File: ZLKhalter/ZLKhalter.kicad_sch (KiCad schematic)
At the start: 4 parts, among them J1 Conn_02x04_Counter_Clockwise, J2 Conn_01x04_Pin, J3 Conn_02x04_Counter_Clockwise

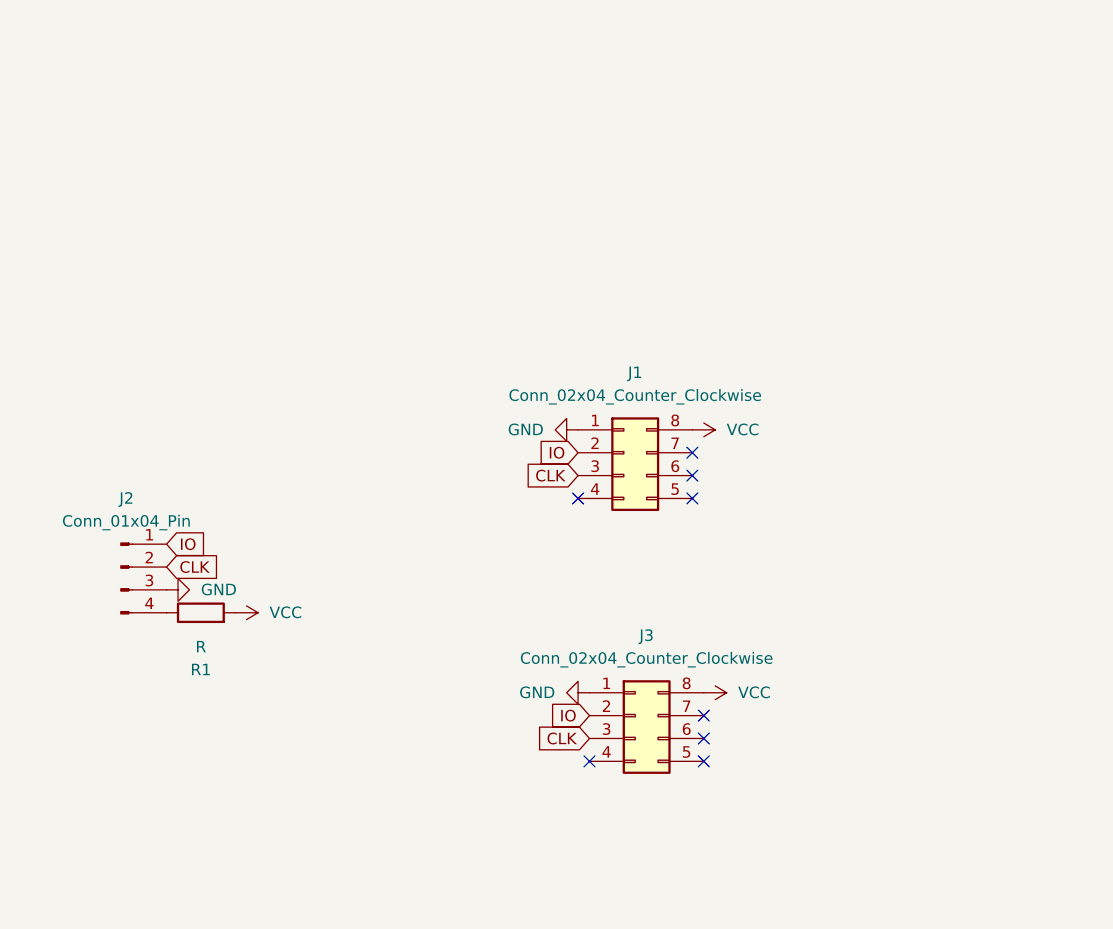
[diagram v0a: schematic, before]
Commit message: kleinerer sim kontakt
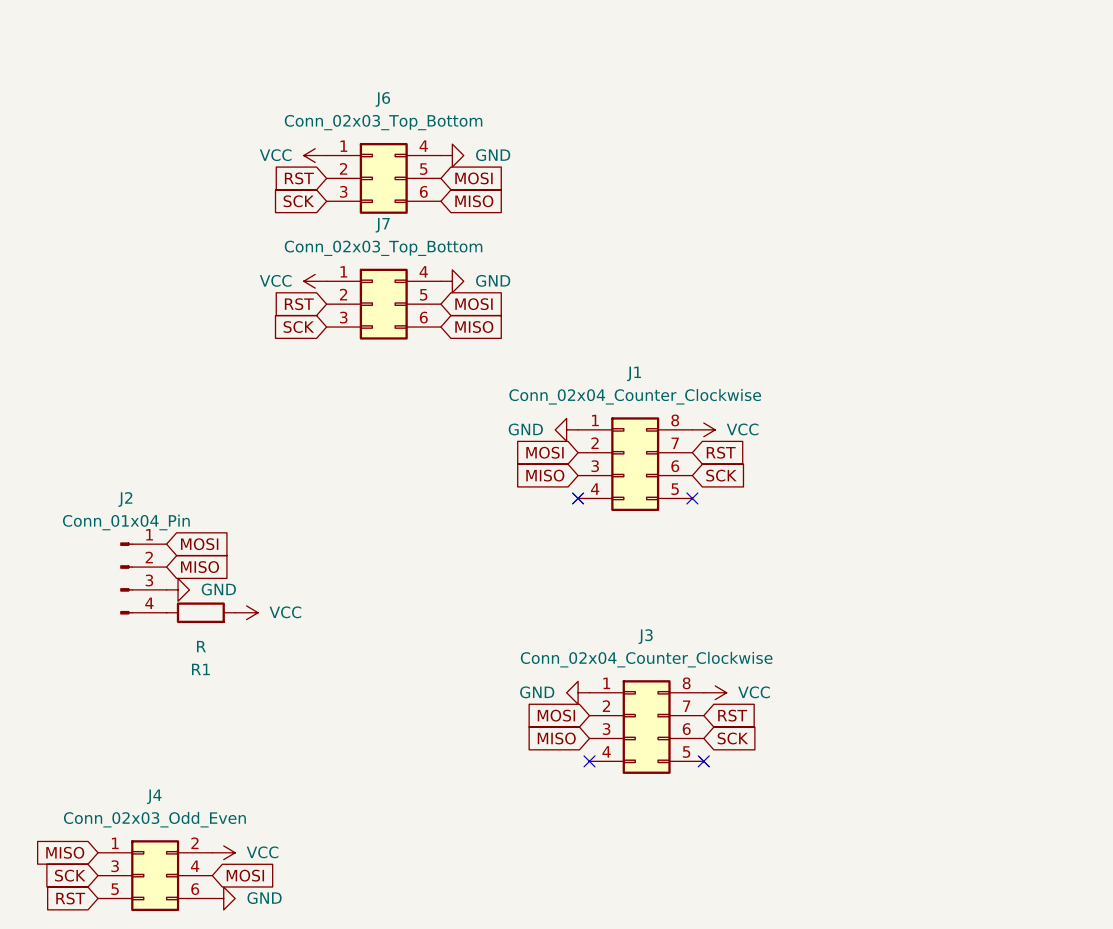
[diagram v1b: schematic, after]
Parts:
- added J4: Conn_02x03_Odd_Even, Connector_IDC:IDC-Header_2x03_P2.54mm_Vertical, symbol Connector_Generic:Conn_02x03_Odd_Even
- added J6, J7: Conn_02x03_Top_Bottom, SIM:4FF-SIM, symbol Connector_Generic:Conn_02x03_Top_Bottom
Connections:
- net GND: now also J4.6 (Pin_6), J6.4 (Pin_4), J7.4 (Pin_4)
- net VCC: now also J4.2 (Pin_2), J6.1 (Pin_1), J7.1 (Pin_1)
- net SCK: now reaches J1.6 (Pin_6)
- net SCK: now also J3.6 (Pin_6), J4.3 (Pin_3), J6.3 (Pin_3), J7.3 (Pin_3)
- net RST: now reaches J1.7 (Pin_7)
- net RST: now also J3.7 (Pin_7), J4.5 (Pin_5), J6.2 (Pin_2), J7.2 (Pin_2)
- net CLK renamed MISO
- net MISO: now also J4.1 (Pin_1), J6.6 (Pin_6), J7.6 (Pin_6)
- net IO renamed MOSI
- net MOSI: now also J4.4 (Pin_4), J6.5 (Pin_5), J7.5 (Pin_5)
- no-connect marks 8 -> 4

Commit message: 12v zlk
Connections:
- net +12V: now reaches J2.4 (Pin_4), R1.1
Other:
- moved on the sheet: J1, J2, J3, J4, J6, J7, R1

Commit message: zlk widerstand
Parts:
- R1: value R -> 270; footprint Resistor_SMD:R_0805_2012Metric -> Resistor_SMD:R_0603_1608Metric_Pad0.98x0.95mm_HandSolder
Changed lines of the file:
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@@
 			)
 		)
-		(property "Value" "R"
+		(property "Value" "270"
 			(at 127 54.61 90)
 			(effects
@@
 			)
 		)
-		(property "Footprint" "Resistor_SMD:R_0805_2012Metric"
+		(property "Footprint" "Resistor_SMD:R_0603_1608Metric_Pad0.98x0.95mm_HandSolder"
 			(at 127 52.578 90)
 			(effects

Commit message: halter sid sod
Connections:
- net MISO renamed SID_MISO
- net MOSI renamed SOD_MOSI
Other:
- moved on the sheet: J6, J7
